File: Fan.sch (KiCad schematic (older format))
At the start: 11 parts, among them Q2 DMN65D8L-7, Q3 AOD476, Q4 AOD476, U11 OPA4170, U8 MCP4801

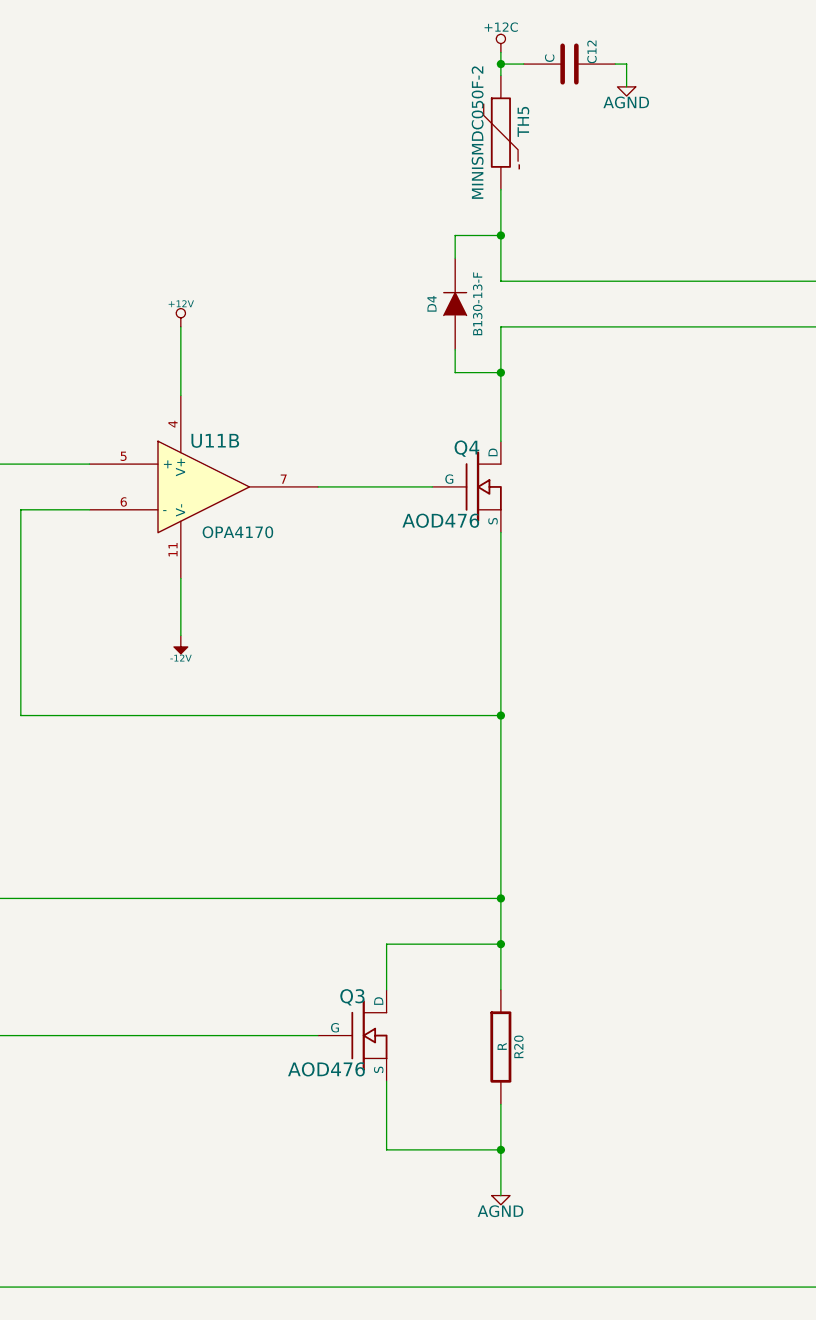
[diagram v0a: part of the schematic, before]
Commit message: Various minor updates after Ground and Power Planes video
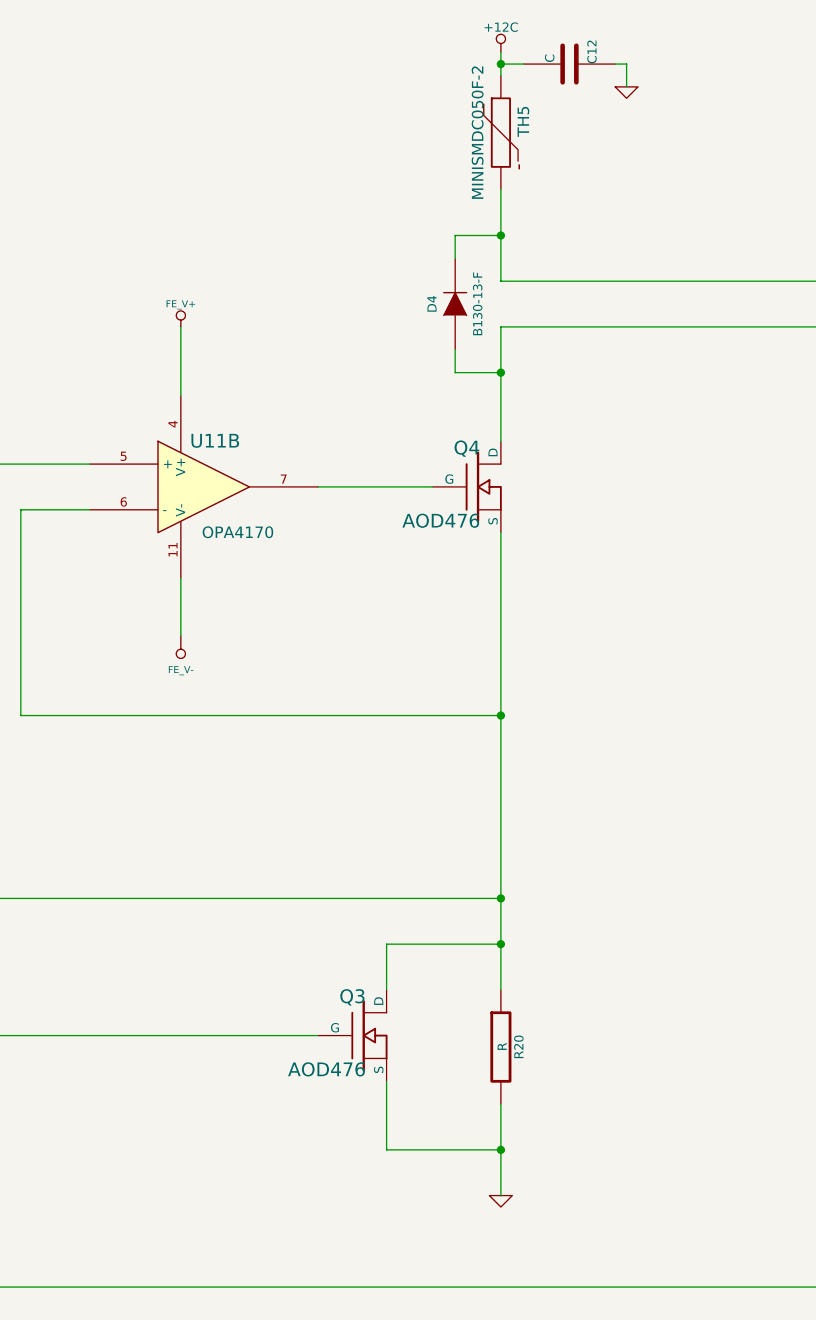
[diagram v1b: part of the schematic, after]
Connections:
- net labels added: FE_V+, FE_V-, GND
- net labels removed: +12V, -12V
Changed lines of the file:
@@
 $EndComp
 $Comp
-L AGND #PWR039
-U 1 1 52F02747
-P 7200 5700
-F 0 "#PWR039" H 7200 5700 40  0001 C CNN
-F 1 "AGND" H 7200 5630 50  0000 C CNN
-F 2 "" H 7200 5700 60  0000 C CNN
-F 3 "" H 7200 5700 60  0000 C CNN
-	1    7200 5700
-	1    0    0    -1
-$EndComp
-$Comp
-L +12V #PWR040
-U 1 1 52F02768
-P 5800 1900
-F 0 "#PWR040" H 5800 1850 20  0001 C CNN
-F 1 "+12V" H 5800 2000 30  0000 C CNN
-F 2 "" H 5800 1900 60  0000 C CNN
-F 3 "" H 5800 1900 60  0000 C CNN
-	1    5800 1900
-	1    0    0    -1
-$EndComp
-$Comp
-L -12V #PWR041
-U 1 1 52F02786
-P 5800 3250
-F 0 "#PWR041" H 5800 3380 20  0001 C CNN
-F 1 "-12V" H 5800 3350 30  0000 C CNN
-F 2 "" H 5800 3250 60  0000 C CNN
-F 3 "" H 5800 3250 60  0000 C CNN
-	1    5800 3250
-	-1   0    0    1
-$EndComp
-$Comp
-L AGND #PWR042
+L AGND #PWR44
 U 1 1 52F0282F
 P 4600 3400
-F 0 "#PWR042" H 4600 3400 40  0001 C CNN
+F 0 "#PWR44" H 4600 3400 40  0001 C CNN
 F 1 "AGND" H 4600 3330 50  0000 C CNN
 F 2 "" H 4600 3400 60  0000 C CNN
@@
 	1500 5000 6400 5000
 $Comp
-L +12C #PWR043
+L +12C #PWR47
 U 1 1 52FBEABF
 P 7200 700
-F 0 "#PWR043" H 7200 670 30  0001 C CNN
+F 0 "#PWR47" H 7200 670 30  0001 C CNN
 F 1 "+12C" H 7200 810 40  0000 C CNN
 F 2 "" H 7200 700 60  0000 C CNN
@@
 	1000 2800 1200 2800
 $Comp
-L +5V #PWR044
+L +5V #PWR42
 U 1 1 530AC1D4
 P 1900 1350
-F 0 "#PWR044" H 1900 1440 20  0001 C CNN
+F 0 "#PWR42" H 1900 1440 20  0001 C CNN
 F 1 "+5V" H 1900 1440 30  0000 C CNN
 F 2 "" H 1900 1350 60  0000 C CNN
@@
 $EndComp
 $Comp
-L AGND #PWR045
+L AGND #PWR41
 U 1 1 530AC1E0
 P 1400 1600
-F 0 "#PWR045" H 1400 1600 40  0001 C CNN
+F 0 "#PWR41" H 1400 1600 40  0001 C CNN
 F 1 "AGND" H 1400 1530 50  0000 C CNN
 F 2 "" H 1400 1600 60  0000 C CNN
@@
 	1900 1350 1900 1700
 $Comp
-L AGND #PWR046
+L AGND #PWR43
 U 1 1 530AC1EB
 P 1900 3450
-F 0 "#PWR046" H 1900 3450 40  0001 C CNN
+F 0 "#PWR43" H 1900 3450 40  0001 C CNN
 F 1 "AGND" H 1900 3380 50  0000 C CNN
 F 2 "" H 1900 3450 60  0000 C CNN
@@
 	1    7500 750
 	0    1    -1   0
-$EndComp
-$Comp
-L AGND #PWR047
-U 1 1 530AD567
-P 7750 850
-F 0 "#PWR047" H 7750 850 40  0001 C CNN
-F 1 "AGND" H 7750 780 50  0000 C CNN
-F 2 "" H 7750 850 60  0000 C CNN
-F 3 "" H 7750 850 60  0000 C CNN
-	1    7750 850
-	-1   0    0    -1
 $EndComp
 Wire Wire Line
@@
 	1    0    0    -1
 $EndComp
+$Comp
+L FE_V- #PWR46
+U 1 1 530BD840
+P 5800 3250
+F 0 "#PWR46" H 5800 3450 40  0001 C CNN
+F 1 "FE_V-" H 5800 3400 30  0000 C CNN
+F 2 "" H 5800 3250 60  0000 C CNN
+F 3 "" H 5800 3250 60  0000 C CNN
+	1    5800 3250
+	-1   0    0    1
+$EndComp
+$Comp
+L FE_V+ #PWR45
+U 1 1 530BD846
+P 5800 1900
+F 0 "#PWR45" H 5800 2000 30  0001 C CNN
+F 1 "FE_V+" H 5800 2000 30  0000 C CNN
+F 2 "" H 5800 1900 60  0000 C CNN
+F 3 "" H 5800 1900 60  0000 C CNN
+	1    5800 1900
+	1    0    0    -1
+$EndComp
+$Comp
+L GND #PWR48
+U 1 1 5313C508
+P 7200 5700
+F 0 "#PWR48" H 7200 5700 30  0001 C CNN
+F 1 "GND" H 7200 5630 30  0001 C CNN
+F 2 "" H 7200 5700 60  0000 C CNN
+F 3 "" H 7200 5700 60  0000 C CNN
+	1    7200 5700
+	1    0    0    -1
+$EndComp
+$Comp
+L GND #PWR49
+U 1 1 5313C524
+P 7750 850
+F 0 "#PWR49" H 7750 850 30  0001 C CNN
+F 1 "GND" H 7750 780 30  0001 C CNN
+F 2 "" H 7750 850 60  0000 C CNN
+F 3 "" H 7750 850 60  0000 C CNN
+	1    7750 850
+	1    0    0    -1
+$EndComp

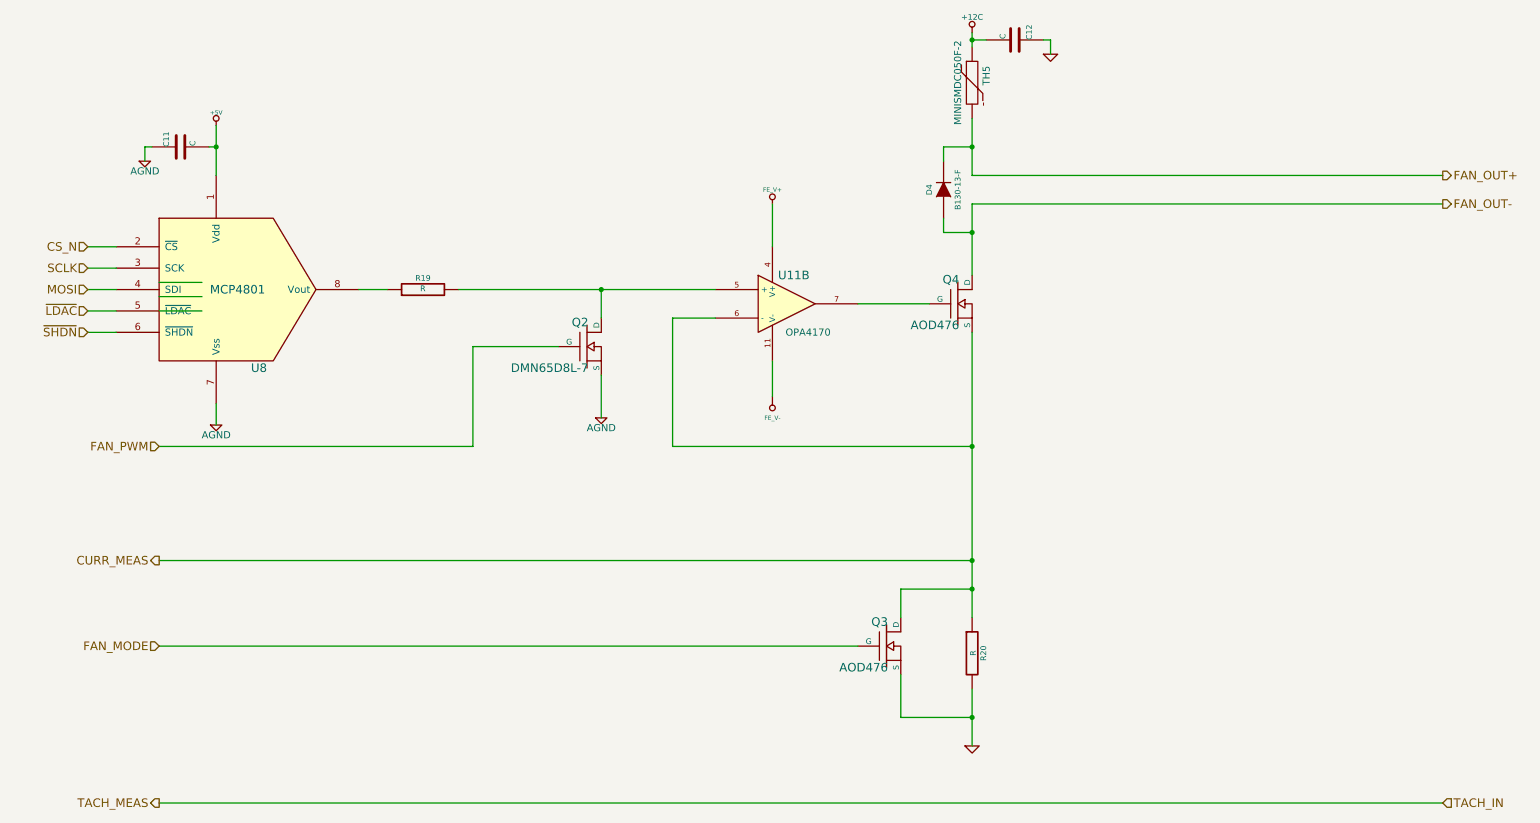
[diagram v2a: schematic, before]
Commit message: Updates from Layout Work Session 4 video
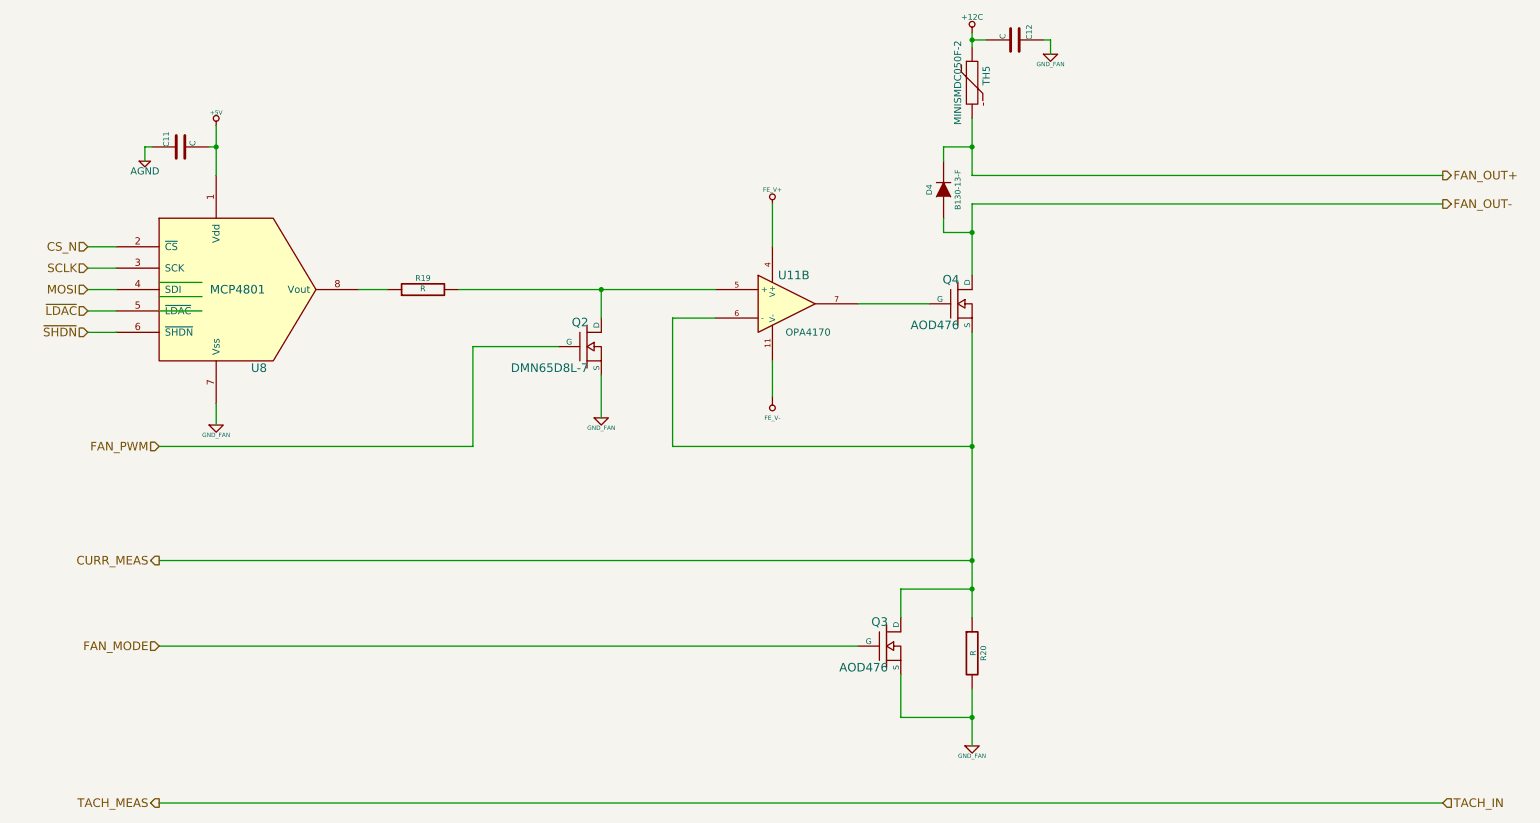
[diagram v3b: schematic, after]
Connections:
- net labels added: GND_FAN
- net labels removed: GND
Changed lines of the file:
@@
-	1    0    0    -1
-$EndComp
-$Comp
-L AGND #PWR038
-U 1 1 52F0282F
-P 4600 3400
-F 0 "#PWR038" H 4600 3400 40  0001 C CNN
-F 1 "AGND" H 4600 3330 50  0000 C CNN
-F 2 "" H 4600 3400 60  0000 C CNN
-F 3 "" H 4600 3400 60  0000 C CNN
-	1    4600 3400
 	1    0    0    -1
 $EndComp
@@
 	1500 5000 6400 5000
 $Comp
-L +12C #PWR039
+L +12C #PWR033
 U 1 1 52FBEABF
 P 7200 700
-F 0 "#PWR039" H 7200 670 30  0001 C CNN
+F 0 "#PWR033" H 7200 670 30  0001 C CNN
 F 1 "+12C" H 7200 810 40  0000 C CNN
 F 2 "" H 7200 700 60  0000 C CNN
@@
 	1000 2800 1200 2800
 $Comp
-L +5V #PWR040
+L +5V #PWR034
 U 1 1 530AC1D4
 P 1900 1350
-F 0 "#PWR040" H 1900 1440 20  0001 C CNN
+F 0 "#PWR034" H 1900 1440 20  0001 C CNN
 F 1 "+5V" H 1900 1440 30  0000 C CNN
 F 2 "" H 1900 1350 60  0000 C CNN
@@
 $EndComp
 $Comp
-L AGND #PWR041
+L AGND #PWR035
 U 1 1 530AC1E0
 P 1400 1600
-F 0 "#PWR041" H 1400 1600 40  0001 C CNN
+F 0 "#PWR035" H 1400 1600 40  0001 C CNN
 F 1 "AGND" H 1400 1530 50  0000 C CNN
 F 2 "" H 1400 1600 60  0000 C CNN
@@
 Wire Wire Line
 	1900 1350 1900 1700
-$Comp
-L AGND #PWR042
-U 1 1 530AC1EB
-P 1900 3450
-F 0 "#PWR042" H 1900 3450 40  0001 C CNN
-F 1 "AGND" H 1900 3380 50  0000 C CNN
-F 2 "" H 1900 3450 60  0000 C CNN
-F 3 "" H 1900 3450 60  0000 C CNN
-	1    1900 3450
-	1    0    0    -1
-$EndComp
 Wire Wire Line
 	1900 3450 1900 3300
@@
 $EndComp
 $Comp
-L FE_V+ #PWR043
+L FE_V+ #PWR036
 U 1 1 530BD846
 P 5800 1900
-F 0 "#PWR043" H 5800 2000 30  0001 C CNN
+F 0 "#PWR036" H 5800 2000 30  0001 C CNN
 F 1 "FE_V+" H 5800 2000 30  0000 C CNN
 F 2 "" H 5800 1900 60  0000 C CNN
@@
 $EndComp
 $Comp
-L GND #PWR044
-U 1 1 5313C508
+L GND_FAN #PWR037
+U 1 1 53151FA9
+P 1900 3450
+F 0 "#PWR037" H 1900 3450 30  0001 C CNN
+F 1 "GND_FAN" H 1900 3380 30  0000 C CNN
+F 2 "" H 1900 3450 60  0000 C CNN
+F 3 "" H 1900 3450 60  0000 C CNN
+	1    1900 3450
+	1    0    0    -1
+$EndComp
+$Comp
+L GND_FAN #PWR038
+U 1 1 53151FBB
+P 4600 3400
+F 0 "#PWR038" H 4600 3400 30  0001 C CNN
+F 1 "GND_FAN" H 4600 3330 30  0000 C CNN
+F 2 "" H 4600 3400 60  0000 C CNN
+F 3 "" H 4600 3400 60  0000 C CNN
+	1    4600 3400
+	1    0    0    -1
+$EndComp
+$Comp
+L GND_FAN #PWR039
+U 1 1 53151FC6
+P 7750 850
+F 0 "#PWR039" H 7750 850 30  0001 C CNN
+F 1 "GND_FAN" H 7750 780 30  0000 C CNN
+F 2 "" H 7750 850 60  0000 C CNN
+F 3 "" H 7750 850 60  0000 C CNN
+	1    7750 850
+	1    0    0    -1
+$EndComp
+$Comp
+L GND_FAN #PWR040
+U 1 1 53151FD1
 P 7200 5700
-F 0 "#PWR044" H 7200 5700 30  0001 C CNN
-F 1 "GND" H 7200 5630 30  0001 C CNN
+F 0 "#PWR040" H 7200 5700 30  0001 C CNN
+F 1 "GND_FAN" H 7200 5630 30  0000 C CNN
 F 2 "" H 7200 5700 60  0000 C CNN
 F 3 "" H 7200 5700 60  0000 C CNN
@@
 	1    0    0    -1
 $EndComp
-$Comp
-L GND #PWR045
-U 1 1 5313C524
-P 7750 850
-F 0 "#PWR045" H 7750 850 30  0001 C CNN
-F 1 "GND" H 7750 780 30  0001 C CNN
-F 2 "" H 7750 850 60  0000 C CNN
-F 3 "" H 7750 850 60  0000 C CNN
-	1    7750 850
-	1    0    0    -1
-$EndComp

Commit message: Updates from Layout Work Session 5 video
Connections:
- net labels removed: GND_FAN
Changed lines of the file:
@@
 	1500 5000 6400 5000
 $Comp
-L +12C #PWR033
+L +12C #PWR034
 U 1 1 52FBEABF
 P 7200 700
-F 0 "#PWR033" H 7200 670 30  0001 C CNN
+F 0 "#PWR034" H 7200 670 30  0001 C CNN
 F 1 "+12C" H 7200 810 40  0000 C CNN
 F 2 "" H 7200 700 60  0000 C CNN
@@
 	1000 2800 1200 2800
 $Comp
-L +5V #PWR034
+L +5V #PWR035
 U 1 1 530AC1D4
 P 1900 1350
-F 0 "#PWR034" H 1900 1440 20  0001 C CNN
+F 0 "#PWR035" H 1900 1440 20  0001 C CNN
 F 1 "+5V" H 1900 1440 30  0000 C CNN
 F 2 "" H 1900 1350 60  0000 C CNN
@@
 $EndComp
 $Comp
-L AGND #PWR035
+L AGND #PWR036
 U 1 1 530AC1E0
 P 1400 1600
-F 0 "#PWR035" H 1400 1600 40  0001 C CNN
+F 0 "#PWR036" H 1400 1600 40  0001 C CNN
 F 1 "AGND" H 1400 1530 50  0000 C CNN
 F 2 "" H 1400 1600 60  0000 C CNN
@@
 $EndComp
 $Comp
-L FE_V+ #PWR036
+L FE_V+ #PWR037
 U 1 1 530BD846
 P 5800 1900
-F 0 "#PWR036" H 5800 2000 30  0001 C CNN
+F 0 "#PWR037" H 5800 2000 30  0001 C CNN
 F 1 "FE_V+" H 5800 2000 30  0000 C CNN
 F 2 "" H 5800 1900 60  0000 C CNN
@@
 $EndComp
 $Comp
-L GND_FAN #PWR037
-U 1 1 53151FA9
+L AGND #PWR038
+U 1 1 53162F09
 P 1900 3450
-F 0 "#PWR037" H 1900 3450 30  0001 C CNN
-F 1 "GND_FAN" H 1900 3380 30  0000 C CNN
+F 0 "#PWR038" H 1900 3450 40  0001 C CNN
+F 1 "AGND" H 1900 3380 50  0000 C CNN
 F 2 "" H 1900 3450 60  0000 C CNN
 F 3 "" H 1900 3450 60  0000 C CNN
@@
 $EndComp
 $Comp
-L GND_FAN #PWR038
-U 1 1 53151FBB
+L AGND #PWR039
+U 1 1 53162F25
 P 4600 3400
-F 0 "#PWR038" H 4600 3400 30  0001 C CNN
-F 1 "GND_FAN" H 4600 3330 30  0000 C CNN
+F 0 "#PWR039" H 4600 3400 40  0001 C CNN
+F 1 "AGND" H 4600 3330 50  0000 C CNN
 F 2 "" H 4600 3400 60  0000 C CNN
 F 3 "" H 4600 3400 60  0000 C CNN
@@
 $EndComp
 $Comp
-L GND_FAN #PWR039
-U 1 1 53151FC6
+L AGND #PWR040
+U 1 1 53162F3A
+P 7200 5700
+F 0 "#PWR040" H 7200 5700 40  0001 C CNN
+F 1 "AGND" H 7200 5630 50  0000 C CNN
+F 2 "" H 7200 5700 60  0000 C CNN
+F 3 "" H 7200 5700 60  0000 C CNN
+	1    7200 5700
+	1    0    0    -1
+$EndComp
+$Comp
+L AGND #PWR041
+U 1 1 53162F4F
 P 7750 850
-F 0 "#PWR039" H 7750 850 30  0001 C CNN
-F 1 "GND_FAN" H 7750 780 30  0000 C CNN
+F 0 "#PWR041" H 7750 850 40  0001 C CNN
+F 1 "AGND" H 7750 780 50  0000 C CNN
 F 2 "" H 7750 850 60  0000 C CNN
 F 3 "" H 7750 850 60  0000 C CNN
@@
 	1    0    0    -1
 $EndComp
-$Comp
-L GND_FAN #PWR040
-U 1 1 53151FD1
-P 7200 5700
-F 0 "#PWR040" H 7200 5700 30  0001 C CNN
-F 1 "GND_FAN" H 7200 5630 30  0000 C CNN
-F 2 "" H 7200 5700 60  0000 C CNN
-F 3 "" H 7200 5700 60  0000 C CNN
-	1    7200 5700
-	1    0    0    -1
-$EndComp
